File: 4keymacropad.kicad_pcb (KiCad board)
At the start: 2 copper layers, 62.2 x 53.3 mm, 9 parts, among them J1 Conn_01x05, SW1 SW_Push, SW2 SW_Push, SW3 SW_Push, SW4 SW_Push

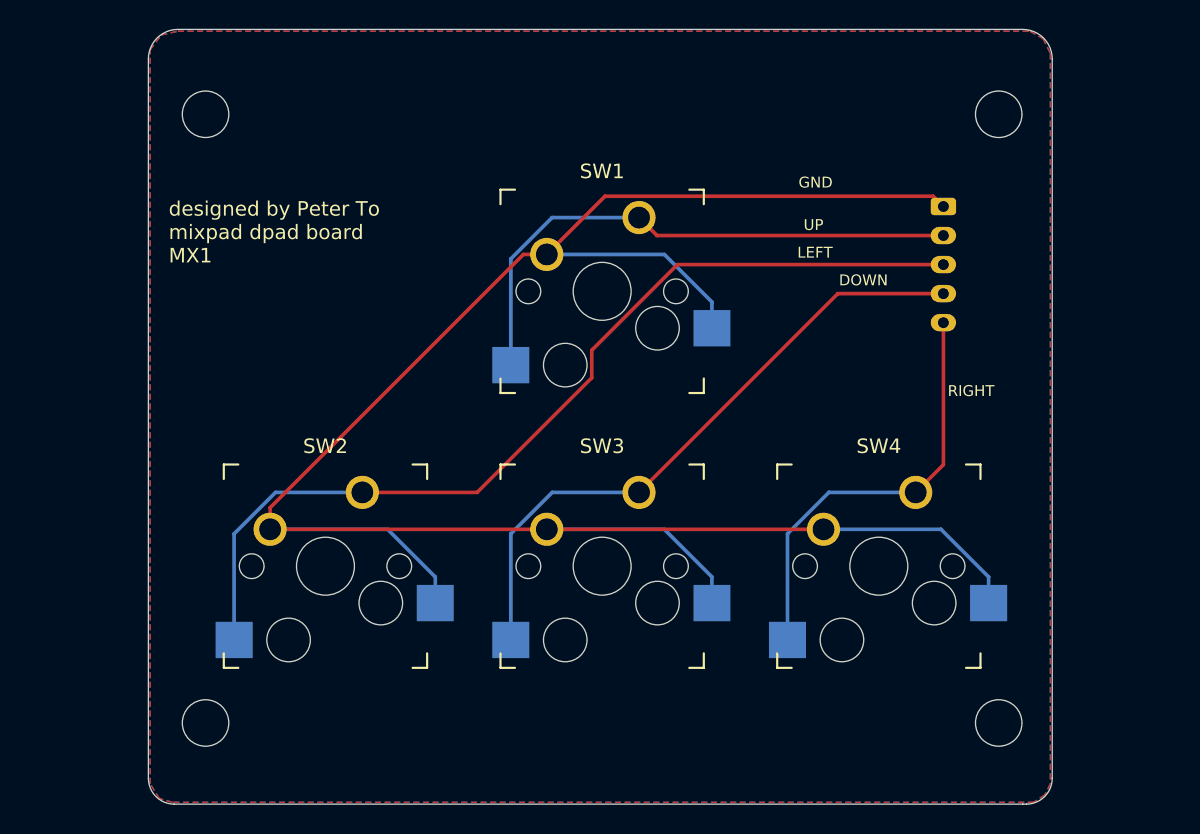
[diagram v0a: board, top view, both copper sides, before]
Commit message: version two of pcb, moves the jst ph to the center and right side of the pcb and change m3 to m2 holes, shrinks length and increases width of pcb, removes top layer ground pour
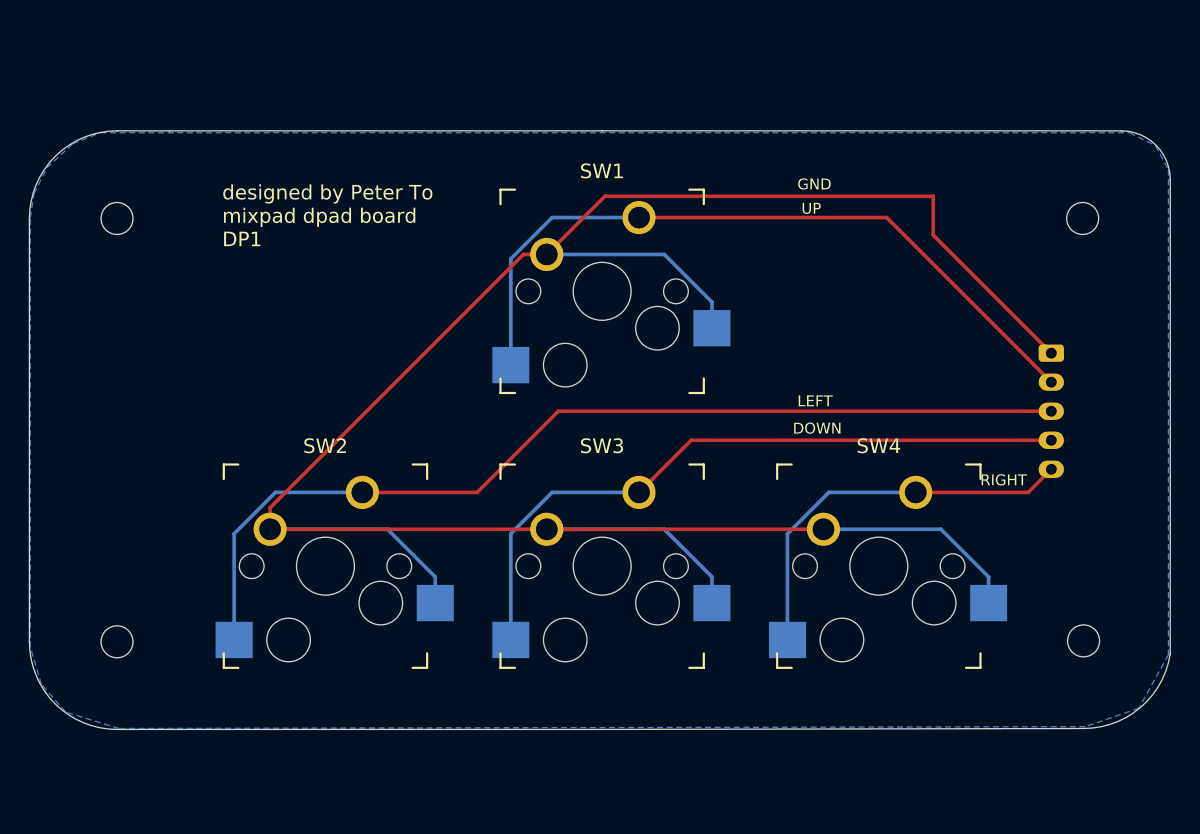
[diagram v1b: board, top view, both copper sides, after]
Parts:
- removed the REF** at (107.3, 69.8)
- removed the REF** at (161.9, 111.8)
- removed the REF** at (161.9, 69.8)
- removed the REF** at (107.3, 111.8)
- added REF**: MountingHole_2.2mm_M2, MountingHole:MountingHole_2.2mm_M2, F.Cu at (101.2, 106.2)
- added REF**: MountingHole_2.2mm_M2, MountingHole:MountingHole_2.2mm_M2, F.Cu at (101.2, 77.0)
- added REF**: MountingHole_2.2mm_M2, MountingHole:MountingHole_2.2mm_M2, F.Cu at (167.8, 106.1)
- added REF**: MountingHole_2.2mm_M2, MountingHole:MountingHole_2.2mm_M2, F.Cu at (167.7, 77.0)
- moved J1 12.5 mm to (165.5, 86.3)
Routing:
- net GND: track 153.8 -> 166.4 mm
- net Net-(J1-Pad2): track 38.8 -> 50.4 mm
- net Net-(J1-Pad4): track 44.2 -> 47.2 mm
- net Net-(J1-Pad5): track 29.8 -> 27.3 mm
- net Net-(J1-Pad3): track 64.9 -> 67.1 mm
- removed copper zone on F.Cu, net GND
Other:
- board size 62.2 x 53.3 mm -> 78.5 x 41.2 mm
- board text added: "designed by Peter To mixpad dpad board DP1"
- board text removed: "designed by Peter To mixpad dpad board MX1"
